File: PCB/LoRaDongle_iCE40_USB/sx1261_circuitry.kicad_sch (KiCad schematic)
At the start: 41 parts, among them J5 142-0701-801, J8 Jumper, U3 SX1261IMLTRT, U4 SKY13587-378LF, Y2 Crystal_GND24

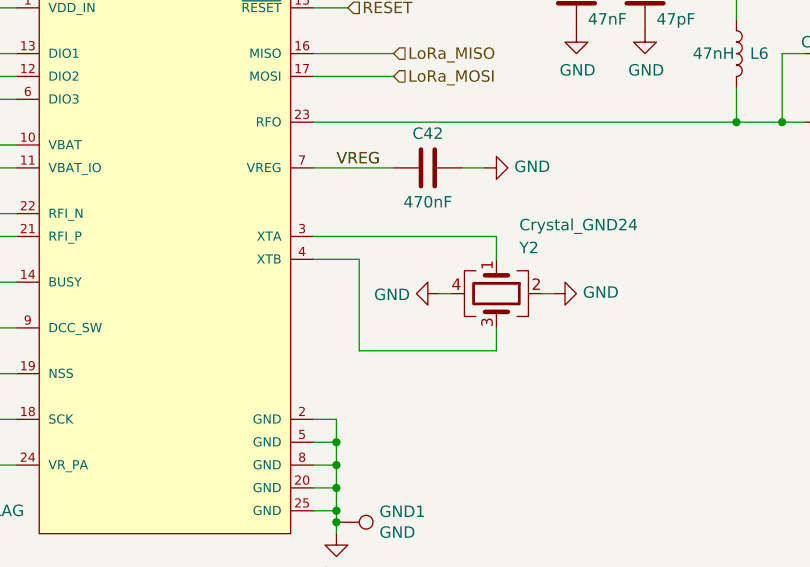
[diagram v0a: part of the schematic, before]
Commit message: updated jumpers, connectors and testpoints
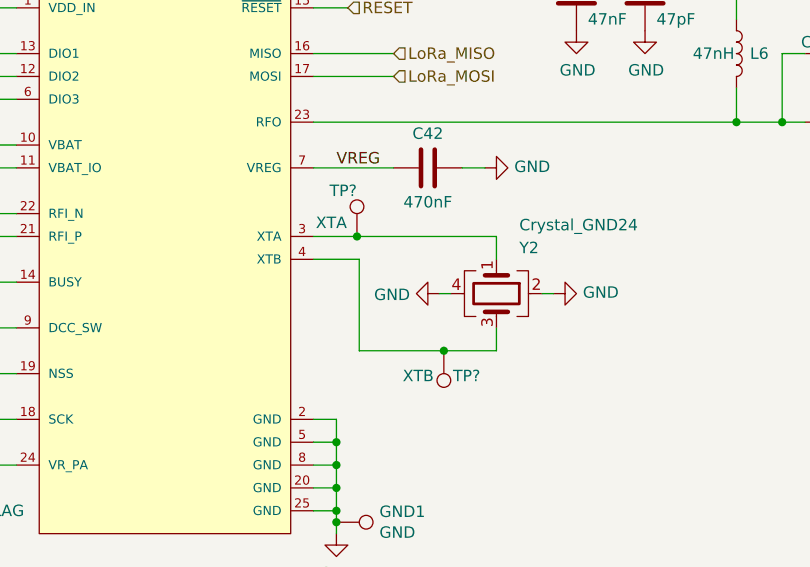
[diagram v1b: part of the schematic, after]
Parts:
- added TP?: XTA, symbol Connector:TestPoint
- added TP?: XTB, symbol Connector:TestPoint
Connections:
- net at U3.3 (XTA), Y2.1: now also TP?.1
- net at U3.4 (XTB), Y2.3: now also TP?.1
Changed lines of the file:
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@@
   (junction (at 143.51 88.9) (diameter 0) (color 0 0 0 0)
   )
+  (junction (at 145.796 60.96) (diameter 0) (color 0 0 0 0)
+  )
   (junction (at 104.14 52.07) (diameter 0) (color 0 0 0 0)
   )
@@
   )
   (junction (at 41.91 38.1) (diameter 0) (color 0 0 0 0)
+  )
+  (junction (at 155.448 73.66) (diameter 0) (color 0 0 0 0)
   )
   (no_connect (at 104.14 45.72))
@@
     (stroke (width 0) (type default) (color 0 0 0 0))
   )
-  (wire (pts (xy 146.05 73.66) (xy 161.29 73.66))
+  (wire (pts (xy 146.05 73.66) (xy 155.448 73.66))
     (stroke (width 0) (type default) (color 0 0 0 0))
   )
@@
     (stroke (width 0) (type default) (color 0 0 0 0))
   )
-  (wire (pts (xy 140.97 60.96) (xy 161.29 60.96))
+  (wire (pts (xy 140.97 60.96) (xy 145.796 60.96))
     (stroke (width 0) (type default) (color 0 0 0 0))
   )
@@
     (stroke (width 0) (type default) (color 0 0 0 0))
   )
+  (wire (pts (xy 145.796 60.96) (xy 161.29 60.96))
+    (stroke (width 0) (type default) (color 0 0 0 0))
+  )
   (wire (pts (xy 38.1 46.99) (xy 38.1 48.26))
     (stroke (width 0) (type default) (color 0 0 0 0))
@@
   )
   (wire (pts (xy 154.94 115.57) (xy 156.21 115.57))
+    (stroke (width 0) (type default) (color 0 0 0 0))
+  )
+  (wire (pts (xy 155.448 73.66) (xy 161.29 73.66))
     (stroke (width 0) (type default) (color 0 0 0 0))
   )
@@
       (effects (font (size 1.27 1.27)) hide)
     )
+    (pin "1")
+  )
+  (symbol (lib_id "Connector:TestPoint") (at 145.796 60.96 0) (unit 1)
+    (in_bom yes) (on_board yes)
+    (property "Reference" "TP?" (id 0) (at 142.748 55.88 0)
+      (effects (font (size 1.27 1.27)) (justify left))
+    )
+    (property "Value" "XTA" (id 1) (at 141.224 59.436 0)
+      (effects (font (size 1.27 1.27)) (justify left))
+    )
+    (property "Footprint" "" (id 2) (at 150.876 60.96 0)
+      (effects (font (size 1.27 1.27)) hide)
+    )
+    (property "Datasheet" "~" (id 3) (at 150.876 60.96 0)
+      (effects (font (size 1.27 1.27)) hide)
+    )
+    (pin "1")
+  )
+  (symbol (lib_id "Connector:TestPoint") (at 155.448 73.66 180) (unit 1)
+    (in_bom yes) (on_board yes)
+    (property "Reference" "TP?" (id 0) (at 156.464 76.454 0)
+      (effects (font (size 1.27 1.27)) (justify right))
+    )
+    (property "Value" "XTB" (id 1) (at 150.876 76.454 0)
+      (effects (font (size 1.27 1.27)) (justify right))
+    )
+    (property "Footprint" "" (id 2) (at 150.368 73.66 0)
+      (effects (font (size 1.27 1.27)) hide)
+    )
+    (property "Datasheet" "~" (id 3) (at 150.368 73.66 0)
+      (effects (font (size 1.27 1.27)) hide)
+    )
